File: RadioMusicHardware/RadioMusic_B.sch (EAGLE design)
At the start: 31 parts, among them IC3 7805L, IC4 TL074, U1 TEENSY_3.1_TW

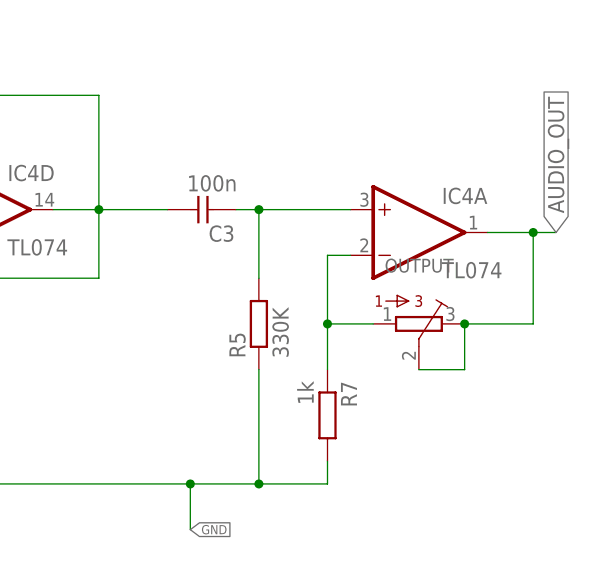
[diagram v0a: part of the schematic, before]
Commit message: Add value to trimmer
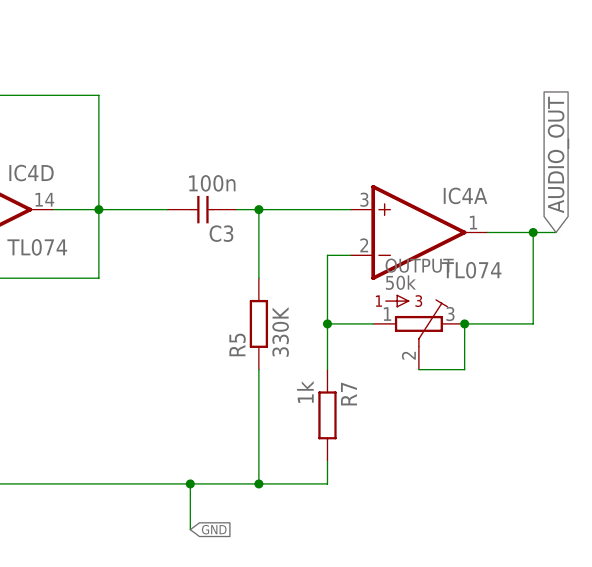
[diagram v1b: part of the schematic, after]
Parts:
- OUTPUT: value (none) -> 50k
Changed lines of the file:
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@@
 <part name="JP1" library="SparkFun-Connectors" deviceset="M11" device="PTH" value="M11PTH"/>
 <part name="JP3" library="SparkFun-Connectors" deviceset="M07" device=""/>
-<part name="OUTPUT" library="bourns" deviceset="3362" device="P"/>
+<part name="OUTPUT" library="bourns" deviceset="3362" device="P" value="50k"/>
 <part name="IC4" library="linear" deviceset="TL074" device="P" value="TL074"/>
 </parts>

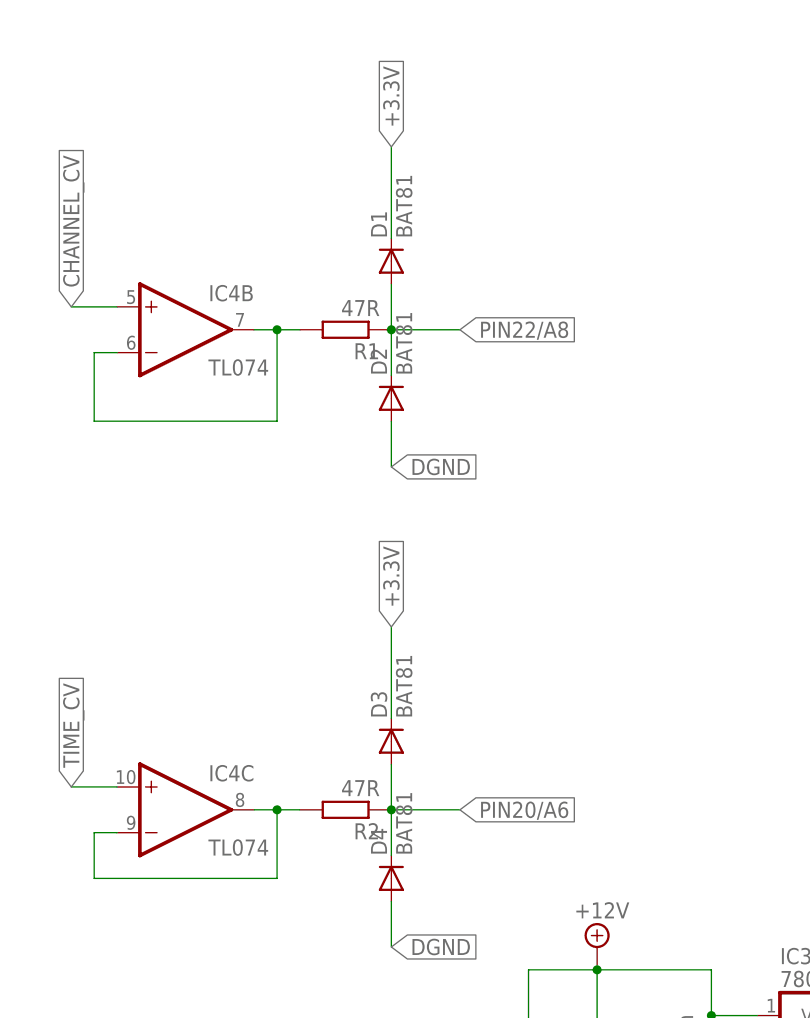
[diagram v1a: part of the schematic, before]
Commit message: Fixed issues on Rev1 proto boards
Diodes changed to BAT42
LED resistors changed to 2k
Ground error on Front board fixed
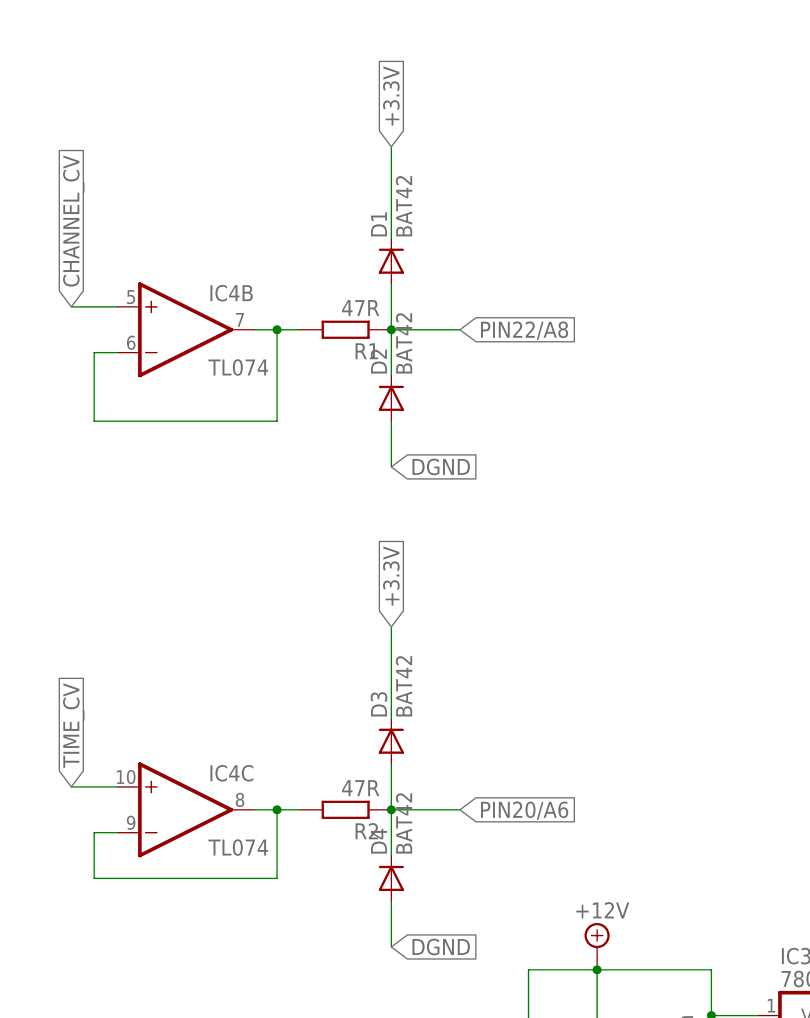
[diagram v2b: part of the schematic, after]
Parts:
- D1, D2, D3, D4: value BAT81 -> BAT42
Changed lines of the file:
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@@
 <part name="U1" library="TomW" deviceset="TEENSY_3.1_TW" device=""/>
 <part name="IC3" library="gm-regulators" deviceset="78*" device="L" technology="05"/>
-<part name="D1" library="diode" deviceset="BAT81" device="" value="BAT81"/>
-<part name="D2" library="diode" deviceset="BAT81" device="" value="BAT81"/>
+<part name="D1" library="diode" deviceset="BAT81" device="" value="BAT42"/>
+<part name="D2" library="diode" deviceset="BAT81" device="" value="BAT42"/>
 <part name="R4" library="TomW" deviceset="R-EU_" device="STANDARD_RESISTOR" value="8.2k"/>
 <part name="R3" library="TomW" deviceset="R-EU_" device="STANDARD_RESISTOR" value="8.2k"/>
@@
 <part name="C2" library="TomW" deviceset="C-EU" device="050-025X075" value="100n"/>
 <part name="R1" library="TomW" deviceset="R-EU_" device="STANDARD_RESISTOR" value="47R"/>
-<part name="D3" library="diode" deviceset="BAT81" device="" value="BAT81"/>
-<part name="D4" library="diode" deviceset="BAT81" device="" value="BAT81"/>
+<part name="D3" library="diode" deviceset="BAT81" device="" value="BAT42"/>
+<part name="D4" library="diode" deviceset="BAT81" device="" value="BAT42"/>
 <part name="R2" library="TomW" deviceset="R-EU_" device="STANDARD_RESISTOR" value="47R"/>
 <part name="L1" library="inductors" deviceset="BL0" device="1RN1A"/>

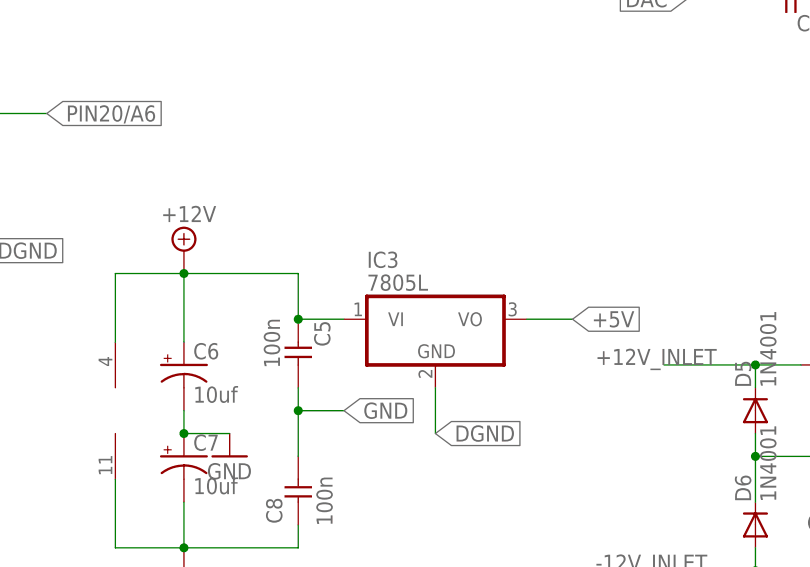
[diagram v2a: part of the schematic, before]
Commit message: Corrected power regulator label
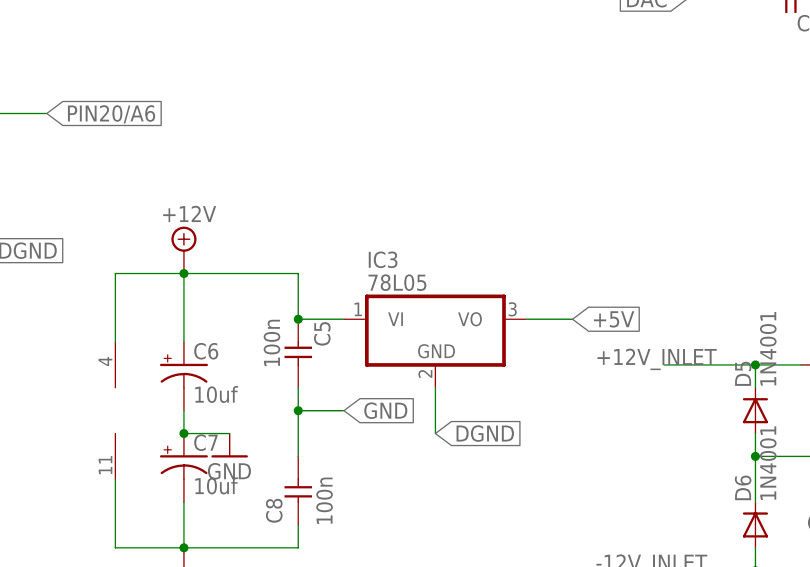
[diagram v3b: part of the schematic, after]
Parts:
- IC3: value 7805L -> 78L05
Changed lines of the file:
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@@
 <part name="SUPPLY2" library="supply2" deviceset="GND" device=""/>
 <part name="U1" library="TomW" deviceset="TEENSY_3.1_TW" device=""/>
-<part name="IC3" library="gm-regulators" deviceset="78*" device="L" technology="05"/>
+<part name="IC3" library="gm-regulators" deviceset="78*" device="L" technology="05" value="78L05"/>
 <part name="D1" library="diode" deviceset="BAT81" device="" value="BAT42"/>
 <part name="D2" library="diode" deviceset="BAT81" device="" value="BAT42"/>

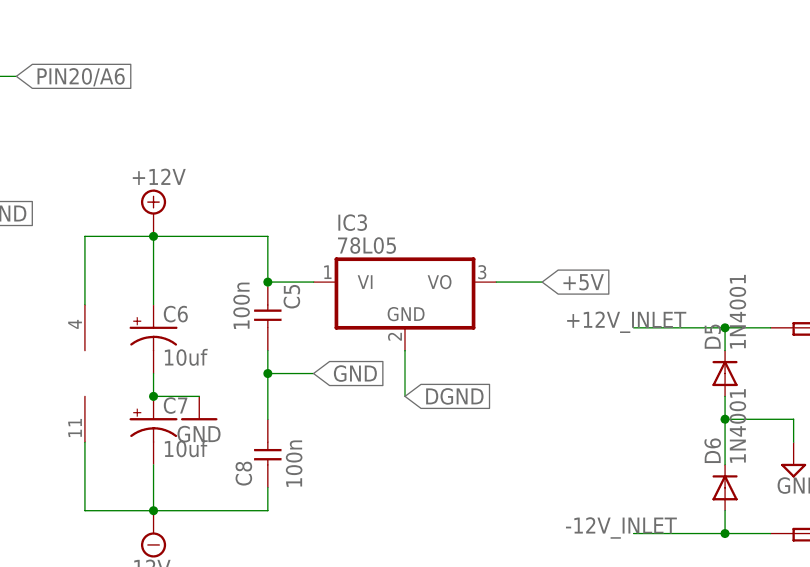
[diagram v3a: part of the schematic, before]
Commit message: Fix Voltage Regulator + cosmetics rear PCB
Fixes #25
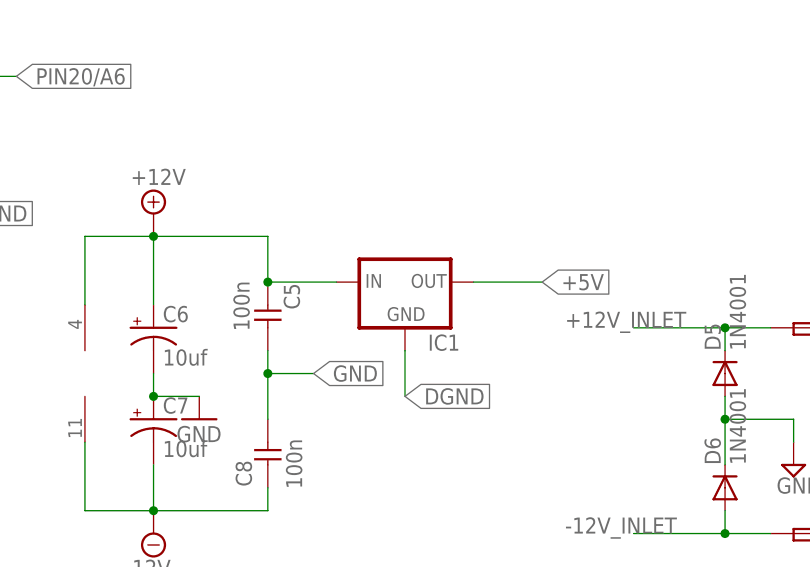
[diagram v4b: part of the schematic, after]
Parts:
- removed IC3: 78L05, gm-regulators:7805L
- added IC1: (no value), v-reg:78LXX
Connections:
- net +12V: now also IC1.IN; no longer IC3.VI
- net +5V: now also IC1.OUT; no longer IC3.VO
- net DGND: now also IC1.GND; no longer IC3.GND
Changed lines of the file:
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@@
 <part name="SUPPLY2" library="supply2" deviceset="GND" device=""/>
 <part name="U1" library="TomW" deviceset="TEENSY_3.1_TW" device=""/>
-<part name="IC3" library="gm-regulators" deviceset="78*" device="L" technology="05" value="78L05"/>
 <part name="D1" library="diode" deviceset="BAT81" device="" value="BAT42"/>
 <part name="D2" library="diode" deviceset="BAT81" device="" value="BAT42"/>
@@
 <part name="OUTPUT" library="bourns" deviceset="3362" device="P" value="50k"/>
 <part name="IC4" library="linear" deviceset="TL074" device="P" value="TL074"/>
+<part name="IC1" library="v-reg" deviceset="78LXX" device=""/>
 </parts>
 <sheets>
@@
 <instance part="IC4" gate="D" x="182.88" y="71.12"/>
 <instance part="IC4" gate="A" x="231.14" y="68.58"/>
-<instance part="IC3" gate="A1" x="91.44" y="38.1"/>
 <instance part="D1" gate="1" x="40.64" y="121.92" rot="R90"/>
 <instance part="D2" gate="1" x="40.64" y="106.68" rot="R90"/>
@@
 <instance part="OUTPUT" gate="G$1" x="231.14" y="58.42" rot="R270"/>
 <instance part="IC4" gate="P" x="55.88" y="27.94"/>
+<instance part="IC1" gate="1" x="91.44" y="38.1"/>
 </instances>
 <busses>
@@
 <wire x1="76.2" y1="43.18" x2="63.5" y2="43.18" width="0.1524" layer="91"/>
 <junction x="63.5" y="43.18"/>
-<pinref part="IC3" gate="A1" pin="VI"/>
-<wire x1="81.28" y1="38.1" x2="76.2" y2="38.1" width="0.1524" layer="91"/>
+<wire x1="83.82" y1="38.1" x2="76.2" y2="38.1" width="0.1524" layer="91"/>
 <junction x="76.2" y="38.1"/>
 <wire x1="55.88" y1="35.56" x2="55.88" y2="43.18" width="0.1524" layer="91"/>
 <wire x1="55.88" y1="43.18" x2="63.5" y2="43.18" width="0.1524" layer="91"/>
 <pinref part="IC4" gate="P" pin="V+"/>
+<pinref part="IC1" gate="1" pin="IN"/>
 </segment>
 <segment>
@@
 <net name="+5V" class="0">
 <segment>
-<pinref part="IC3" gate="A1" pin="VO"/>
-<wire x1="106.68" y1="38.1" x2="101.6" y2="38.1" width="0.1524" layer="91"/>
+<wire x1="106.68" y1="38.1" x2="99.06" y2="38.1" width="0.1524" layer="91"/>
 <label x="106.68" y="38.1" size="1.778" layer="95" xref="yes"/>
+<pinref part="IC1" gate="1" pin="OUT"/>
 </segment>
 <segment>
@@
 </segment>
 <segment>
-<pinref part="IC3" gate="A1" pin="GND"/>
 <wire x1="91.44" y1="25.4" x2="91.44" y2="30.48" width="0.1524" layer="91"/>
 <label x="91.44" y="25.4" size="1.778" layer="95" xref="yes"/>
-</segment>
-</net>
+<pinref part="IC1" gate="1" pin="GND"/>
+</segment>
+</net>
